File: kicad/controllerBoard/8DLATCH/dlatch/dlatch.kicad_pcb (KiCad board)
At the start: 2 copper layers, 12 parts, among them Q1 Q_PMOS_GSD, Q10 Q_NMOS_GSD, Q11 Q_PMOS_GSD, Q12 Q_NMOS_GSD, Q2 Q_NMOS_GSD, Q3 Q_PMOS_GSD, Q4 Q_NMOS_GSD, Q5 Q_PMOS_GSD, Q6 Q_NMOS_GSD, Q7 Q_PMOS_GSD, Q8 Q_NMOS_GSD, Q9 Q_PMOS_GSD

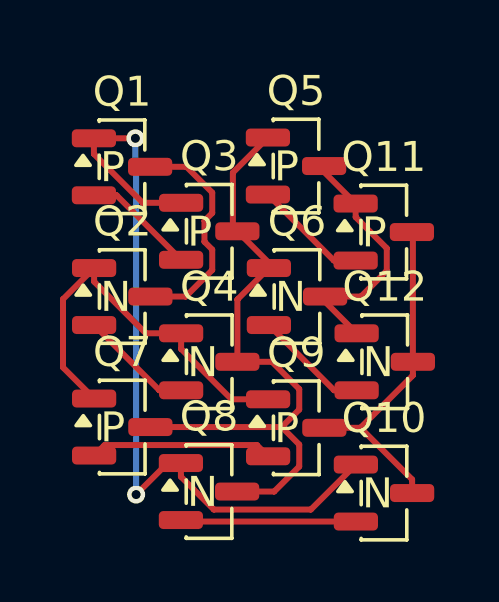
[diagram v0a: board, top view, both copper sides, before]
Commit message: add mounting holes
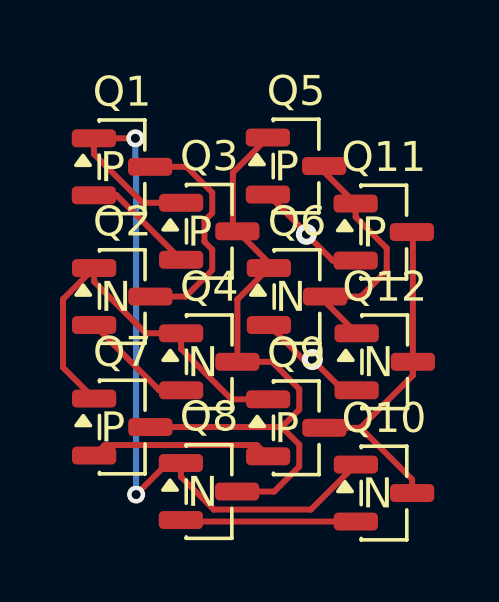
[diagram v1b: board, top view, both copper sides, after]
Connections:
- net Net-(Q11-S) renamed +5V
- net Net-(Q12-S) renamed GND
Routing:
- net +5V: track 3.84 -> 3.86 mm, vias 0 -> 1
- net GND: vias 0 -> 1
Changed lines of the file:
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@@
 	)
 	(setup
+		(stackup
+			(layer "F.SilkS"
+				(type "Top Silk Screen")
+			)
+			(layer "F.Paste"
+				(type "Top Solder Paste")
+			)
+			(layer "F.Mask"
+				(type "Top Solder Mask")
+				(thickness 0.01)
+			)
+			(layer "F.Cu"
+				(type "copper")
+				(thickness 0.035)
+			)
+			(layer "dielectric 1"
+				(type "core")
+				(thickness 1.51)
+				(material "FR4")
+				(epsilon_r 4.5)
+				(loss_tangent 0.02)
+			)
+			(layer "B.Cu"
+				(type "copper")
+				(thickness 0.035)
+			)
+			(layer "B.Mask"
+				(type "Bottom Solder Mask")
+				(thickness 0.01)
+			)
+			(layer "B.Paste"
+				(type "Bottom Solder Paste")
+			)
+			(layer "B.SilkS"
+				(type "Bottom Silk Screen")
+			)
+			(copper_finish "None")
+			(dielectric_constraints no)
+		)
 		(pad_to_mask_clearance 0)
 		(allow_soldermask_bridges_in_footprints no)
@@
 		(capping no)
 		(filling no)
+		(zone_defaults)
 		(pcbplotparams
 			(layerselection 0x00000000_00000000_55555555_5755f5ff)
@@
 			(layers "F.Cu" "F.Mask" "F.Paste")
 			(roundrect_rratio 0.25)
-			(net "Net-(Q11-S)")
+			(net "+5V")
 			(pinfunction "S_2")
 			(pintype "passive")
@@
 			(layers "F.Cu" "F.Mask" "F.Paste")
 			(roundrect_rratio 0.25)
-			(net "Net-(Q11-S)")
+			(net "+5V")
 			(pinfunction "S_2")
 			(pintype "passive")
@@
 			(layers "F.Cu" "F.Mask" "F.Paste")
 			(roundrect_rratio 0.25)
-			(net "Net-(Q12-S)")
+			(net "GND")
 			(pinfunction "S_2")
 			(pintype "passive")
@@
 			(layers "F.Cu" "F.Mask" "F.Paste")
 			(roundrect_rratio 0.25)
-			(net "Net-(Q12-S)")
+			(net "GND")
 			(pinfunction "S_2")
 			(pintype "passive")
@@
 	)
 	(segment
-		(start 107.6175 70.75)
-		(end 109.8175 72.95)
-		(width 0.2)
-		(layer "F.Cu")
-		(net "Net-(Q11-S)")
-	)
-	(segment
-		(start 109.8175 72.95)
-		(end 110.5425 72.95)
-		(width 0.2)
-		(layer "F.Cu")
-		(net "Net-(Q11-S)")
-	)
-	(segment
 		(start 112.45 76.778052)
 		(end 112.45 76.325)
@@
 	)
 	(segment
-		(start 109.825 77.275)
+		(start 108.9 72.0325)
+		(end 107.6175 70.75)
+		(width 0.2)
+		(layer "F.Cu")
+		(net "+5V")
+	)
+	(segment
+		(start 110.5425 72.95)
+		(end 109.775 72.95)
+		(width 0.2)
+		(layer "F.Cu")
+		(net "+5V")
+	)
+	(segment
+		(start 109.775 72.95)
+		(end 108.9 72.075)
+		(width 0.2)
+		(layer "F.Cu")
+		(net "+5V")
+	)
+	(segment
+		(start 108.9 72.075)
+		(end 108.9 72.0325)
+		(width 0.2)
+		(layer "F.Cu")
+		(net "+5V")
+	)
+	(via
+		(at 108.9 72.075)
+		(size 0.7)
+		(drill 0.3)
+		(layers "F.Cu" "B.Cu")
+		(net "+5V")
+	)
+	(segment
+		(start 108.8 76.25)
 		(end 107.65 75.1)
 		(width 0.2)
 		(layer "F.Cu")
-		(net "Net-(Q12-S)")
+		(net "GND")
+	)
+	(segment
+		(start 109.1 76.25)
+		(end 108.8 76.25)
+		(width 0.2)
+		(layer "F.Cu")
+		(net "GND")
 	)
 	(segment
 		(start 110.575 77.275)
-		(end 109.825 77.275)
+		(end 110.125 77.275)
 		(width 0.2)
 		(layer "F.Cu")
-		(net "Net-(Q12-S)")
+		(net "GND")
+	)
+	(segment
+		(start 110.125 77.275)
+		(end 109.1 76.25)
+		(width 0.2)
+		(layer "F.Cu")
+		(net "GND")
+	)
+	(via
+		(at 109.1 76.25)
+		(size 0.7)
+		(drill 0.3)
+		(layers "F.Cu" "B.Cu")
+		(net "GND")
 	)
 	(embedded_fonts no)
